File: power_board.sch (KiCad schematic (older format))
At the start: 31 parts, among them CON1 MICROUSB, J1 Conn_02x03_Odd_Even, J2 Conn_01x01, J3 Conn_01x01, J4 Conn_01x01, SW1 SW_Push, U1 PCA9555PW, U2 ATMEGA328P-AU, U3 PCA9555PW, U4 FT232RL, Y1 Crystal

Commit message: ICs positioning
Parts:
- D1, D2, D3: footprint lsts-discretes:LED_0603 -> LED_SMD:LED_0603_1608Metric
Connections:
- net MTR1_BW: now also U1.10 (IO0_6); no longer U1.6 (IO0_2)
- net MTR1_EN: now also U1.11 (IO0_7); no longer U1.4 (IO0_0)
- net MTR1_FW: now also U1.9 (IO0_5); no longer U1.5 (IO0_1)
- net MTR2_BW: now also U1.19 (IO1_6); no longer U1.9 (IO0_5)
- net MTR2_EN: now also U1.18 (IO1_5); no longer U1.7 (IO0_3)
- net MTR2_FW: now also U1.20 (IO1_7); no longer U1.8 (IO0_4)
- net MTR3_BW: now also U1.16 (IO1_3); no longer U1.13 (IO1_0)
- net MTR3_EN: now also U1.15 (IO1_2); no longer U1.10 (IO0_6)
- net MTR3_FW: now also U1.17 (IO1_4); no longer U1.11 (IO0_7)
- net MTR4_BW: now also U3.5 (IO0_1); no longer U1.16 (IO1_3)
- net MTR4_EN: now also U3.6 (IO0_2); no longer U1.14 (IO1_1)
- net MTR4_FW: now also U3.4 (IO0_0); no longer U1.15 (IO1_2)
- net MTR5_BW: now also U3.8 (IO0_4); no longer U1.19 (IO1_6)
- net MTR5_EN: now also U3.9 (IO0_5); no longer U1.17 (IO1_4)
- net MTR5_FW: now also U3.7 (IO0_3); no longer U1.18 (IO1_5)
- net MTR6_BW: now also U3.19 (IO1_6); no longer U3.6 (IO0_2)
- net MTR6_EN: now also U3.18 (IO1_5); no longer U3.4 (IO0_0)
- net MTR6_FW: now also U3.20 (IO1_7); no longer U3.5 (IO0_1)
- net MTR7_BW: now also U3.16 (IO1_3); no longer U3.9 (IO0_5)
- net MTR7_EN: now also U3.15 (IO1_2); no longer U3.7 (IO0_3)
- net MTR7_FW: now also U3.17 (IO1_4); no longer U3.8 (IO0_4)
- net MTR8_EN: now also U3.11 (IO0_7); no longer U3.10 (IO0_6)
- net MTR8_FW: now also U3.14 (IO1_1); no longer U3.11 (IO0_7)
- net RLY1_EN: now also U1.4 (IO0_0); no longer U3.14 (IO1_1)
- net RLY2_EN: now also U1.5 (IO0_1); no longer U3.15 (IO1_2)
- net RLY3_EN: now also U1.6 (IO0_2); no longer U3.16 (IO1_3)
- net RLY4_EN: now also U1.7 (IO0_3); no longer U3.17 (IO1_4)
- net RLY5_EN: now also U1.8 (IO0_4); no longer U3.18 (IO1_5)
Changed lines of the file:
@@
 F 0 "D2" V 10589 2733 50  0000 R CNN
 F 1 "LED" V 10498 2733 50  0000 R CNN
-F 2 "lsts-discretes:LED_0603" H 10550 2850 50  0001 C CNN
+F 2 "LED_SMD:LED_0603_1608Metric" H 10550 2850 50  0001 C CNN
 F 3 "~" H 10550 2850 50  0001 C CNN
 	1    10550 2850
@@
 F 0 "D3" V 10897 2928 50  0000 L CNN
 F 1 "LED" V 10988 2928 50  0000 L CNN
-F 2 "lsts-discretes:LED_0603" H 10950 2850 50  0001 C CNN
+F 2 "LED_SMD:LED_0603_1608Metric" H 10950 2850 50  0001 C CNN
 F 3 "~" H 10950 2850 50  0001 C CNN
 	1    10950 2850
@@
 SCL
 Wire Wire Line
+	2250 5900 2400 5900
+Wire Wire Line
+	2250 5700 2400 5700
+Wire Wire Line
+	2250 5800 2400 5800
+Wire Wire Line
+	2250 6600 2400 6600
+Wire Wire Line
+	2250 6700 2400 6700
+Wire Wire Line
+	2250 6300 2400 6300
+Wire Wire Line
+	2250 6500 2400 6500
+Wire Wire Line
+	4750 5200 4900 5200
+Wire Wire Line
+	4750 5300 4900 5300
+Wire Wire Line
+	4750 5400 4900 5400
+Wire Wire Line
+	4750 5500 4900 5500
+Wire Wire Line
+	4750 5600 4900 5600
+Wire Wire Line
+	4750 5700 4900 5700
+Wire Wire Line
 	2250 5200 2400 5200
 Wire Wire Line
@@
 Wire Wire Line
 	2250 5600 2400 5600
-Wire Wire Line
-	2250 5700 2400 5700
-Wire Wire Line
-	2250 5800 2400 5800
-Wire Wire Line
-	2250 5900 2400 5900
-Wire Wire Line
-	2250 6100 2400 6100
-Wire Wire Line
-	2250 6200 2400 6200
-Wire Wire Line
-	2250 6300 2400 6300
-Wire Wire Line
-	2250 6400 2400 6400
-Wire Wire Line
-	2250 6500 2400 6500
-Wire Wire Line
-	2250 6600 2400 6600
-Wire Wire Line
-	2250 6700 2400 6700
-Wire Wire Line
-	4750 6200 4900 6200
-Wire Wire Line
-	4750 6300 4900 6300
-Wire Wire Line
-	4750 6400 4900 6400
-Wire Wire Line
-	4750 6500 4900 6500
-Wire Wire Line
-	4750 6600 4900 6600
-Text Label 2400 5200 0    50   ~ 0
+Text Label 2400 5900 0    50   ~ 0
 MTR1_EN
-Text Label 2400 5300 0    50   ~ 0
+Text Label 2400 5700 0    50   ~ 0
 MTR1_FW
-Text Label 2400 5400 0    50   ~ 0
+Text Label 2400 5800 0    50   ~ 0
 MTR1_BW
 Text Label 7200 5000 2    50   ~ 0
@@
 Text Label 9800 5100 2    50   ~ 0
 RLY5_EN
+Text Label 2400 6600 0    50   ~ 0
+MTR2_EN
+Text Label 2400 6700 0    50   ~ 0
+MTR2_BW
+Text Label 2400 6300 0    50   ~ 0
+MTR3_EN
+Text Label 2400 6500 0    50   ~ 0
+MTR3_FW
+Text Label 4900 5400 0    50   ~ 0
+MTR4_EN
+Text Label 4900 5200 0    50   ~ 0
+MTR4_FW
+Text Label 4900 5300 0    50   ~ 0
+MTR4_BW
+Text Label 4900 5700 0    50   ~ 0
+MTR5_EN
+Text Label 4900 5500 0    50   ~ 0
+MTR5_FW
+Text Label 4900 5600 0    50   ~ 0
+MTR5_BW
+Text Label 2400 5200 0    50   ~ 0
+RLY1_EN
+Text Label 2400 5300 0    50   ~ 0
+RLY2_EN
+Text Label 2400 5400 0    50   ~ 0
+RLY3_EN
 Text Label 2400 5500 0    50   ~ 0
-MTR2_EN
+RLY4_EN
 Text Label 2400 5600 0    50   ~ 0
-MTR2_FW
-Text Label 2400 5700 0    50   ~ 0
-MTR2_BW
-Text Label 2400 5800 0    50   ~ 0
-MTR3_EN
-Text Label 2400 5900 0    50   ~ 0
-MTR3_FW
-Text Label 2400 6100 0    50   ~ 0
-MTR3_BW
-Text Label 2400 6200 0    50   ~ 0
-MTR4_EN
-Text Label 2400 6300 0    50   ~ 0
-MTR4_FW
-Text Label 2400 6400 0    50   ~ 0
-MTR4_BW
-Text Label 2400 6500 0    50   ~ 0
-MTR5_EN
-Text Label 2400 6600 0    50   ~ 0
-MTR5_FW
-Text Label 2400 6700 0    50   ~ 0
-MTR5_BW
-Text Label 4900 6200 0    50   ~ 0
-RLY1_EN
-Text Label 4900 6300 0    50   ~ 0
-RLY2_EN
-Text Label 4900 6400 0    50   ~ 0
-RLY3_EN
-Text Label 4900 6500 0    50   ~ 0
-RLY4_EN
-Text Label 4900 6600 0    50   ~ 0
 RLY5_EN
 $Comp
@@
 NoConn ~ 3750 5500
 NoConn ~ 1250 5500
-NoConn ~ 2250 6800
 NoConn ~ 950  2950
 NoConn ~ 950  2850
@@
 F 0 "D1" V 4897 3528 50  0000 L CNN
 F 1 "LED" V 4988 3528 50  0000 L CNN
-F 2 "lsts-discretes:LED_0603" H 4950 3450 50  0001 C CNN
+F 2 "LED_SMD:LED_0603_1608Metric" H 4950 3450 50  0001 C CNN
 F 3 "~" H 4950 3450 50  0001 C CNN
 	1    4950 3450
@@
 $EndComp
 Wire Wire Line
-	4750 5200 4900 5200
-Wire Wire Line
-	4750 5300 4900 5300
-Wire Wire Line
-	4750 5400 4900 5400
-Text Label 4900 5200 0    50   ~ 0
+	4750 6800 4900 6800
+Wire Wire Line
+	4750 6700 4900 6700
+Wire Wire Line
+	4750 6600 4900 6600
+Text Label 4900 6600 0    50   ~ 0
 MTR6_EN
-Text Label 4900 5300 0    50   ~ 0
+Text Label 4900 6800 0    50   ~ 0
 MTR6_FW
-Text Label 4900 5400 0    50   ~ 0
+Text Label 4900 6700 0    50   ~ 0
 MTR6_BW
 Wire Wire Line
-	4750 5500 4900 5500
-Wire Wire Line
-	4750 5600 4900 5600
-Wire Wire Line
-	4750 5700 4900 5700
-Text Label 4900 5500 0    50   ~ 0
+	4750 5900 4900 5900
+Wire Wire Line
+	4750 6100 4900 6100
+Wire Wire Line
+	4750 6200 4900 6200
+Text Label 4900 6300 0    50   ~ 0
 MTR7_EN
-Text Label 4900 5600 0    50   ~ 0
+Text Label 4900 6500 0    50   ~ 0
 MTR7_FW
-Text Label 4900 5700 0    50   ~ 0
+Text Label 4900 6400 0    50   ~ 0
 MTR7_BW
 Wire Wire Line
-	4750 5800 4900 5800
-Wire Wire Line
-	4750 5900 4900 5900
-Wire Wire Line
-	4750 6100 4900 6100
-Text Label 4900 5800 0    50   ~ 0
+	4750 6300 4900 6300
+Wire Wire Line
+	4750 6400 4900 6400
+Wire Wire Line
+	4750 6500 4900 6500
+Text Label 4900 5900 0    50   ~ 0
 MTR8_EN
-Text Label 4900 5900 0    50   ~ 0
+Text Label 4900 6200 0    50   ~ 0
 MTR8_FW
 Text Label 4900 6100 0    50   ~ 0
 MTR8_BW
-NoConn ~ 4750 6700
-NoConn ~ 4750 6800
 Wire Wire Line
 	950  1200 950  1500
@@
 Wire Wire Line
 	6700 7200 6700 7400
+NoConn ~ 2250 6100
+NoConn ~ 2250 6200
+Text Label 2400 6800 0    50   ~ 0
+MTR2_FW
+Wire Wire Line
+	2250 6800 2400 6800
+Text Label 2400 6400 0    50   ~ 0
+MTR3_BW
+Wire Wire Line
+	2250 6400 2400 6400
+NoConn ~ 4750 5800
 $EndSCHEMATC

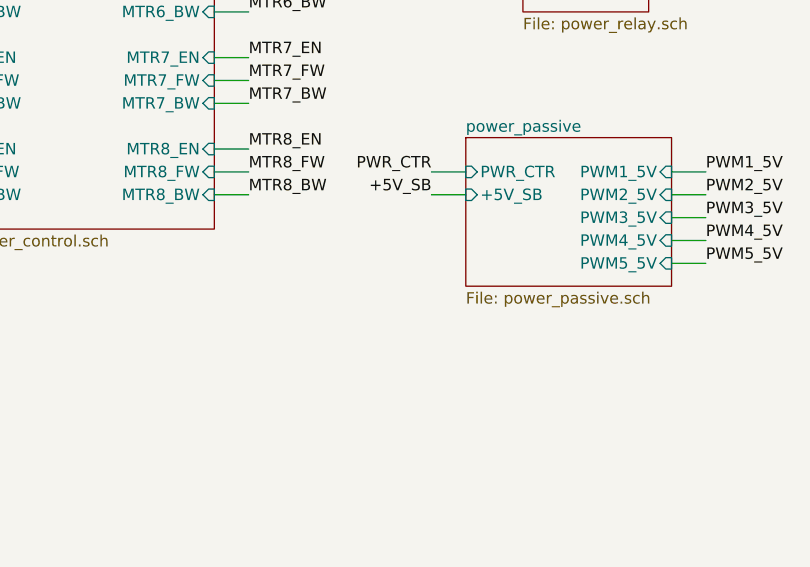
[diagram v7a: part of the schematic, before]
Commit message: Added 47uF electrolytic capacitor to 5V_SB.
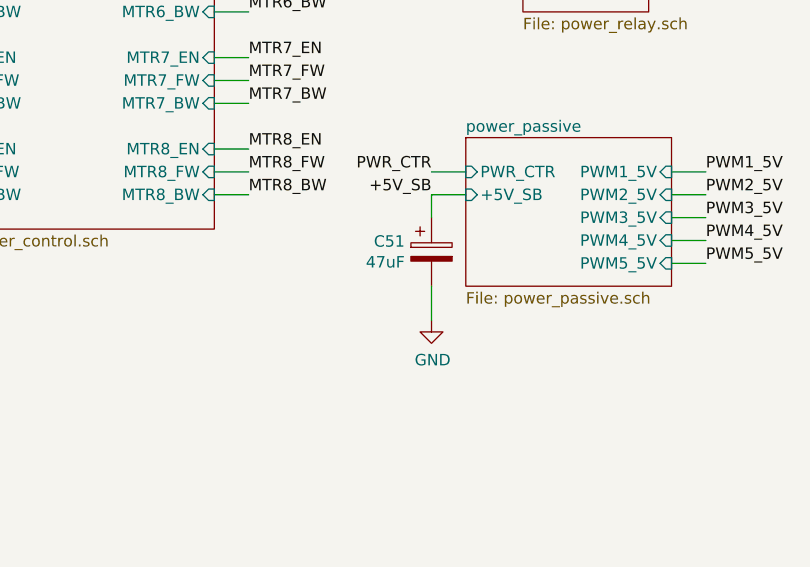
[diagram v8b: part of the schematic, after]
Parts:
- added C51: 47uF, Capacitor_THT:CP_Radial_D5.0mm_P2.00mm, symbol Device:CP
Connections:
- net +5V_SB: now also C51.1
- net GND: now also C51.2
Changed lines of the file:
@@
 	2250 6400 2400 6400
 NoConn ~ 4750 5800
+Wire Wire Line
+	9550 6400 9550 6550
+$Comp
+L power:GND #PWR0102
+U 1 1 5E358472
+P 9550 6550
+F 0 "#PWR0102" H 9550 6300 50  0001 C CNN
+F 1 "GND" H 9555 6377 50  0000 C CNN
+F 2 "" H 9550 6550 50  0001 C CNN
+F 3 "" H 9550 6550 50  0001 C CNN
+	1    9550 6550
+	1    0    0    -1
+$EndComp
+Wire Wire Line
+	9550 6000 9550 6100
+$Comp
+L Device:CP C51
+U 1 1 5E37B7B3
+P 9550 6250
+F 0 "C51" H 9433 6296 50  0000 R CNN
+F 1 "47uF" H 9433 6205 50  0000 R CNN
+F 2 "Capacitor_THT:CP_Radial_D5.0mm_P2.00mm" H 9588 6100 50  0001 C CNN
+F 3 "https://www.we-online.com/catalog/datasheet/860010272003.pdf" H 9550 6250 50  0001 C CNN
+F 4 "860010272003" H 9550 6250 50  0001 C CNN "manf#"
+	1    9550 6250
+	1    0    0    -1
+$EndComp
 $EndSCHEMATC
